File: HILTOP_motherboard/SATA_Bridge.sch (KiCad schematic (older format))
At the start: 36 parts

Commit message: Furthe progress on Schematics, assigned all main footprints using latest libraries, removed unwanted tracking and parts from original PCB layout
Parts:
- C204, C223: renamed from C?; footprint Capacitors_SMD:C_0603 -> Capacitor_SMD:C_0603_1608Metric
- FB10, FB11, FB6, FB7, FB9: renamed from FB?; footprint Resistors_SMD:R_0603 -> Resistor_SMD:R_0603_1608Metric
- R177: renamed from R?; footprint (none) -> Resistor_SMD:R_0603_1608Metric
- U37: renamed from U?; footprint Housings_DFN_QFN:Texas_WQFN-MR-100 -> Devtank_PCB_Lib:PQFP-64_7x7mm_P0.4mm_EP; Devtank (none) -> 118-003
- gave numbers to parts that had none: 27

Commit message: Schematics complete - 1st draft
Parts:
- removed C204, C206, C219: 100nF, Capacitor_SMD:C_0603_1608Metric, symbol C
- removed C208: 1uF, Capacitor_SMD:C_0603_1608Metric, symbol C
- removed C210, C217: 22uF, Capacitor_SMD:C_0805_2012Metric, symbol C
- removed FB10, FB6: 120R_100MHz, Resistor_SMD:R_0603_1608Metric, symbol L
- removed R177: R, Resistor_SMD:R_0603_1608Metric, symbol R
- removed U37: TUSB9260, Devtank_PCB_Lib:PQFP-64_7x7mm_P0.4mm_EP, symbol TUSB9260
- added C204, C206: 9pF, Capacitor_SMD:C_0603_1608Metric, symbol device:C
- added C208, C210: 100nF, Capacitor_SMD:C_0603_1608Metric, symbol device:C
- added D84: STPS1L30, Diode_SMD:D_SMB, symbol device:D
- added D85, D86, D87, D88, D89, D90, D91, D92: GRN, LED_SMD:LED_0603_1608Metric, symbol device:LED
- added J25: DEBUG, Connector_PinHeader_2.54mm:PinHeader_1x03_P2.54mm_Vertical, symbol Connector:Conn_01x03
- added R177, R225, R227, R229: DNF, Resistor_SMD:R_0603_1608Metric, symbol device:R
- added R224, R226, R230, R231: 4K7, Resistor_SMD:R_0603_1608Metric, symbol device:R
- added R228, R233: 10K, Resistor_SMD:R_0603_1608Metric, symbol device:R
- added R232: 0R, Resistor_SMD:R_0603_1608Metric, symbol device:R
- added R234: 90.9K, Resistor_SMD:R_0603_1608Metric, symbol device:R
- added R235, R236, R237, R238, R239, R240, R241, R242: 330R, Resistor_SMD:R_0603_1608Metric, symbol device:R
- added U37: TUSB9261, Devtank_PCB_Lib:PQFP-64_7x7mm_P0.4mm_EP, symbol Devtank:TUSB9261
- added U38: AT25DN512CSSHF-B, Package_SO:SOIC-8_3.9x4.9mm_P1.27mm, symbol memory:AT25_EEPROM
- added Y7: 40MHz Crystal, Crystal:Crystal_SMD_SeikoEpson_FA238V-4Pin_3.2x2.5mm, symbol device:Crystal_GND24
- C195, C196, C197, C198, C199, C200, C201, C202, C203, C205, C207, C209, C211, C212, C213, C214, C215, C216, C218, C220, C221, C222, C223: symbol C -> device:C
- FB11, FB7, FB9: symbol L -> device:L
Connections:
- net labels added: +1V1_SATA, +5V, GPIO_0, GPIO_1, GPIO_2, GPIO_3, GPIO_4, GPIO_5, GPIO_6, GPIO_7
- net labels removed: +1V2_SATA, +1V2_USB2_SATA, +1V8, +1V8_SATA
- wire segments 70 -> 272
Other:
- note added: "Match Tracks to 2.5 Mils\n100Ohms Differential Impedance\n50Ohms Single-ended Impedance"

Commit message: BOM nearly complete!
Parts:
- C195: Devtank (none) -> 105-012
- C196, C221, C222: Devtank (none) -> 105-018
- C197, C198, C199, C200: footprint Resistor_SMD:R_0402_1005Metric -> Capacitor_SMD:C_0402_1005Metric; Devtank (none) -> 105-017
- D85, D86, D87, D88, D89, D90, D91, D92: footprint LED_SMD:LED_0603_1608Metric -> LED_SMD:LED_0402_1005Metric; Devtank (none) -> 110-005
- R235, R236, R237, R238, R239, R240, R241, R242: footprint Resistor_SMD:R_0603_1608Metric -> Resistor_SMD:R_0402_1005Metric
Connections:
- no-connect marks 0 -> 15
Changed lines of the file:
@@
 F 0 "C197" V 2900 1900 50  0000 L CNN
 F 1 "10nF" V 2900 2275 50  0000 L CNN
-F 2 "Resistor_SMD:R_0402_1005Metric" H 2988 2025 50  0001 C CNN
+F 2 "Capacitor_SMD:C_0402_1005Metric" H 2988 2025 50  0001 C CNN
 F 3 "" H 2950 2175 50  0001 C CNN
+F 4 "105-017" V 2950 2175 50  0001 C CNN "Devtank"
 	1    2950 2175
 	0    1    1    0
@@
 F 0 "C198" V 2900 2125 50  0000 L CNN
 F 1 "10nF" V 2900 2500 50  0000 L CNN
-F 2 "Resistor_SMD:R_0402_1005Metric" H 2988 2250 50  0001 C CNN
+F 2 "Capacitor_SMD:C_0402_1005Metric" H 2988 2250 50  0001 C CNN
 F 3 "" H 2950 2400 50  0001 C CNN
+F 4 "105-017" V 2950 2400 50  0001 C CNN "Devtank"
 	1    2950 2400
 	0    1    1    0
@@
 F 0 "C199" V 2900 2350 50  0000 L CNN
 F 1 "10nF" V 2900 2725 50  0000 L CNN
-F 2 "Resistor_SMD:R_0402_1005Metric" H 2988 2475 50  0001 C CNN
+F 2 "Capacitor_SMD:C_0402_1005Metric" H 2988 2475 50  0001 C CNN
 F 3 "" H 2950 2625 50  0001 C CNN
+F 4 "105-017" V 2950 2625 50  0001 C CNN "Devtank"
 	1    2950 2625
 	0    1    1    0
@@
 F 0 "C200" V 2900 2575 50  0000 L CNN
 F 1 "10nF" V 2900 2950 50  0000 L CNN
-F 2 "Resistor_SMD:R_0402_1005Metric" H 2988 2700 50  0001 C CNN
+F 2 "Capacitor_SMD:C_0402_1005Metric" H 2988 2700 50  0001 C CNN
 F 3 "" H 2950 2850 50  0001 C CNN
+F 4 "105-017" V 2950 2850 50  0001 C CNN "Devtank"
 	1    2950 2850
 	0    1    1    0
@@
 F 2 "Capacitor_SMD:C_0805_2012Metric" H 8063 9950 50  0001 C CNN
 F 3 "" H 8025 10100 50  0000 C CNN
+F 4 "105-018" H 8025 10100 50  0001 C CNN "Devtank"
 	1    8025 10100
 	1    0    0    -1
@@
 F 2 "Capacitor_SMD:C_0805_2012Metric" H 8863 9950 50  0001 C CNN
 F 3 "" H 8825 10100 50  0000 C CNN
+F 4 "105-018" H 8825 10100 50  0001 C CNN "Devtank"
 	1    8825 10100
 	1    0    0    -1
@@
 F 2 "Capacitor_SMD:C_0805_2012Metric" H 2688 8100 50  0001 C CNN
 F 3 "" H 2650 8250 50  0000 C CNN
+F 4 "105-018" H 2650 8250 50  0001 C CNN "Devtank"
 	1    2650 8250
 	1    0    0    -1
@@
 F 2 "Capacitor_SMD:C_0603_1608Metric" H 2338 8100 50  0001 C CNN
 F 3 "" H 2300 8250 50  0000 C CNN
+F 4 "105-012" H 2300 8250 50  0001 C CNN "Devtank"
 	1    2300 8250
 	1    0    0    -1
@@
 F 0 "R235" V 11375 6400 50  0000 C CNN
 F 1 "330R" V 11375 6850 50  0000 C CNN
-F 2 "Resistor_SMD:R_0603_1608Metric" V 11355 6625 50  0001 C CNN
+F 2 "Resistor_SMD:R_0402_1005Metric" V 11355 6625 50  0001 C CNN
 F 3 "" H 11425 6625 50  0000 C CNN
 F 4 "101-024" V 11425 6625 60  0001 C CNN "Devtank"
@@
 F 0 "D85" H 10425 6675 50  0000 C CNN
 F 1 "GRN" H 10850 6675 50  0000 C CNN
-F 2 "LED_SMD:LED_0603_1608Metric" H 10625 6625 50  0001 C CNN
+F 2 "LED_SMD:LED_0402_1005Metric" H 10625 6625 50  0001 C CNN
 F 3 "" H 10625 6625 50  0001 C CNN
+F 4 "110-005" H 10625 6625 50  0001 C CNN "Devtank"
 	1    10625 6625
 	1    0    0    -1
@@
 F 0 "R236" V 11375 6600 50  0000 C CNN
 F 1 "330R" V 11375 7050 50  0000 C CNN
-F 2 "Resistor_SMD:R_0603_1608Metric" V 11355 6825 50  0001 C CNN
+F 2 "Resistor_SMD:R_0402_1005Metric" V 11355 6825 50  0001 C CNN
 F 3 "" H 11425 6825 50  0000 C CNN
 F 4 "101-024" V 11425 6825 60  0001 C CNN "Devtank"
@@
 F 0 "D86" H 10425 6875 50  0000 C CNN
 F 1 "GRN" H 10850 6875 50  0000 C CNN
-F 2 "LED_SMD:LED_0603_1608Metric" H 10625 6825 50  0001 C CNN
+F 2 "LED_SMD:LED_0402_1005Metric" H 10625 6825 50  0001 C CNN
 F 3 "" H 10625 6825 50  0001 C CNN
+F 4 "110-005" H 10625 6825 50  0001 C CNN "Devtank"
 	1    10625 6825
 	1    0    0    -1
@@
 F 0 "R237" V 11375 6800 50  0000 C CNN
 F 1 "330R" V 11375 7250 50  0000 C CNN
-F 2 "Resistor_SMD:R_0603_1608Metric" V 11355 7025 50  0001 C CNN
+F 2 "Resistor_SMD:R_0402_1005Metric" V 11355 7025 50  0001 C CNN
 F 3 "" H 11425 7025 50  0000 C CNN
 F 4 "101-024" V 11425 7025 60  0001 C CNN "Devtank"
@@
 F 0 "D87" H 10425 7075 50  0000 C CNN
 F 1 "GRN" H 10850 7075 50  0000 C CNN
-F 2 "LED_SMD:LED_0603_1608Metric" H 10625 7025 50  0001 C CNN
+F 2 "LED_SMD:LED_0402_1005Metric" H 10625 7025 50  0001 C CNN
 F 3 "" H 10625 7025 50  0001 C CNN
+F 4 "110-005" H 10625 7025 50  0001 C CNN "Devtank"
 	1    10625 7025
 	1    0    0    -1
@@
 F 0 "R238" V 11375 7000 50  0000 C CNN
 F 1 "330R" V 11375 7450 50  0000 C CNN
-F 2 "Resistor_SMD:R_0603_1608Metric" V 11355 7225 50  0001 C CNN
+F 2 "Resistor_SMD:R_0402_1005Metric" V 11355 7225 50  0001 C CNN
 F 3 "" H 11425 7225 50  0000 C CNN
 F 4 "101-024" V 11425 7225 60  0001 C CNN "Devtank"
@@
 F 0 "D88" H 10425 7275 50  0000 C CNN
 F 1 "GRN" H 10850 7275 50  0000 C CNN
-F 2 "LED_SMD:LED_0603_1608Metric" H 10625 7225 50  0001 C CNN
+F 2 "LED_SMD:LED_0402_1005Metric" H 10625 7225 50  0001 C CNN
 F 3 "" H 10625 7225 50  0001 C CNN
+F 4 "110-005" H 10625 7225 50  0001 C CNN "Devtank"
 	1    10625 7225
 	1    0    0    -1
@@
 F 0 "R239" V 11375 7200 50  0000 C CNN
 F 1 "330R" V 11375 7650 50  0000 C CNN
-F 2 "Resistor_SMD:R_0603_1608Metric" V 11355 7425 50  0001 C CNN
+F 2 "Resistor_SMD:R_0402_1005Metric" V 11355 7425 50  0001 C CNN
 F 3 "" H 11425 7425 50  0000 C CNN
 F 4 "101-024" V 11425 7425 60  0001 C CNN "Devtank"
@@
 F 0 "D89" H 10425 7475 50  0000 C CNN
 F 1 "GRN" H 10850 7475 50  0000 C CNN
-F 2 "LED_SMD:LED_0603_1608Metric" H 10625 7425 50  0001 C CNN
+F 2 "LED_SMD:LED_0402_1005Metric" H 10625 7425 50  0001 C CNN
 F 3 "" H 10625 7425 50  0001 C CNN
+F 4 "110-005" H 10625 7425 50  0001 C CNN "Devtank"
 	1    10625 7425
 	1    0    0    -1
@@
 F 0 "R240" V 11375 7400 50  0000 C CNN
 F 1 "330R" V 11375 7850 50  0000 C CNN
-F 2 "Resistor_SMD:R_0603_1608Metric" V 11355 7625 50  0001 C CNN
+F 2 "Resistor_SMD:R_0402_1005Metric" V 11355 7625 50  0001 C CNN
 F 3 "" H 11425 7625 50  0000 C CNN
 F 4 "101-024" V 11425 7625 60  0001 C CNN "Devtank"
@@
 F 0 "D90" H 10425 7675 50  0000 C CNN
 F 1 "GRN" H 10850 7675 50  0000 C CNN
-F 2 "LED_SMD:LED_0603_1608Metric" H 10625 7625 50  0001 C CNN
+F 2 "LED_SMD:LED_0402_1005Metric" H 10625 7625 50  0001 C CNN
 F 3 "" H 10625 7625 50  0001 C CNN
+F 4 "110-005" H 10625 7625 50  0001 C CNN "Devtank"
 	1    10625 7625
 	1    0    0    -1
@@
 F 0 "R241" V 11375 7600 50  0000 C CNN
 F 1 "330R" V 11375 8050 50  0000 C CNN
-F 2 "Resistor_SMD:R_0603_1608Metric" V 11355 7825 50  0001 C CNN
+F 2 "Resistor_SMD:R_0402_1005Metric" V 11355 7825 50  0001 C CNN
 F 3 "" H 11425 7825 50  0000 C CNN
 F 4 "101-024" V 11425 7825 60  0001 C CNN "Devtank"
@@
 F 0 "D91" H 10425 7875 50  0000 C CNN
 F 1 "GRN" H 10850 7875 50  0000 C CNN
-F 2 "LED_SMD:LED_0603_1608Metric" H 10625 7825 50  0001 C CNN
+F 2 "LED_SMD:LED_0402_1005Metric" H 10625 7825 50  0001 C CNN
 F 3 "" H 10625 7825 50  0001 C CNN
+F 4 "110-005" H 10625 7825 50  0001 C CNN "Devtank"
 	1    10625 7825
 	1    0    0    -1
@@
 F 0 "R242" V 11375 7800 50  0000 C CNN
 F 1 "330R" V 11375 8250 50  0000 C CNN
-F 2 "Resistor_SMD:R_0603_1608Metric" V 11355 8025 50  0001 C CNN
+F 2 "Resistor_SMD:R_0402_1005Metric" V 11355 8025 50  0001 C CNN
 F 3 "" H 11425 8025 50  0000 C CNN
 F 4 "101-024" V 11425 8025 60  0001 C CNN "Devtank"
@@
 F 0 "D92" H 10425 8075 50  0000 C CNN
 F 1 "GRN" H 10850 8075 50  0000 C CNN
-F 2 "LED_SMD:LED_0603_1608Metric" H 10625 8025 50  0001 C CNN
+F 2 "LED_SMD:LED_0402_1005Metric" H 10625 8025 50  0001 C CNN
 F 3 "" H 10625 8025 50  0001 C CNN
+F 4 "110-005" H 10625 8025 50  0001 C CNN "Devtank"
 	1    10625 8025
 	1    0    0    -1
@@
 Wire Wire Line
 	6875 8425 6875 8700
+NoConn ~ 7975 3250
+NoConn ~ 7975 3350
+NoConn ~ 7975 3450
+NoConn ~ 7975 3550
+NoConn ~ 7975 5250
+NoConn ~ 7975 5350
+NoConn ~ 7975 5550
+NoConn ~ 7975 5650
+NoConn ~ 4100 4050
+NoConn ~ 4100 4150
+NoConn ~ 4100 4400
+NoConn ~ 4100 4500
+NoConn ~ 4100 5575
+NoConn ~ 4900 6250
+NoConn ~ 5200 6250
 $EndSCHEMATC

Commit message: nearly finished placing all parts!
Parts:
- J25: Devtank (none) -> 710-015
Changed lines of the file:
@@
 F 2 "Connector_PinHeader_2.54mm:PinHeader_1x03_P2.54mm_Vertical" H 2675 3950 50  0001 C CNN
 F 3 "" H 2675 3950 50  0001 C CNN
+F 4 "710-015" H 2675 3950 50  0001 C CNN "Devtank"
 	1    2675 3950
 	-1   0    0    -1

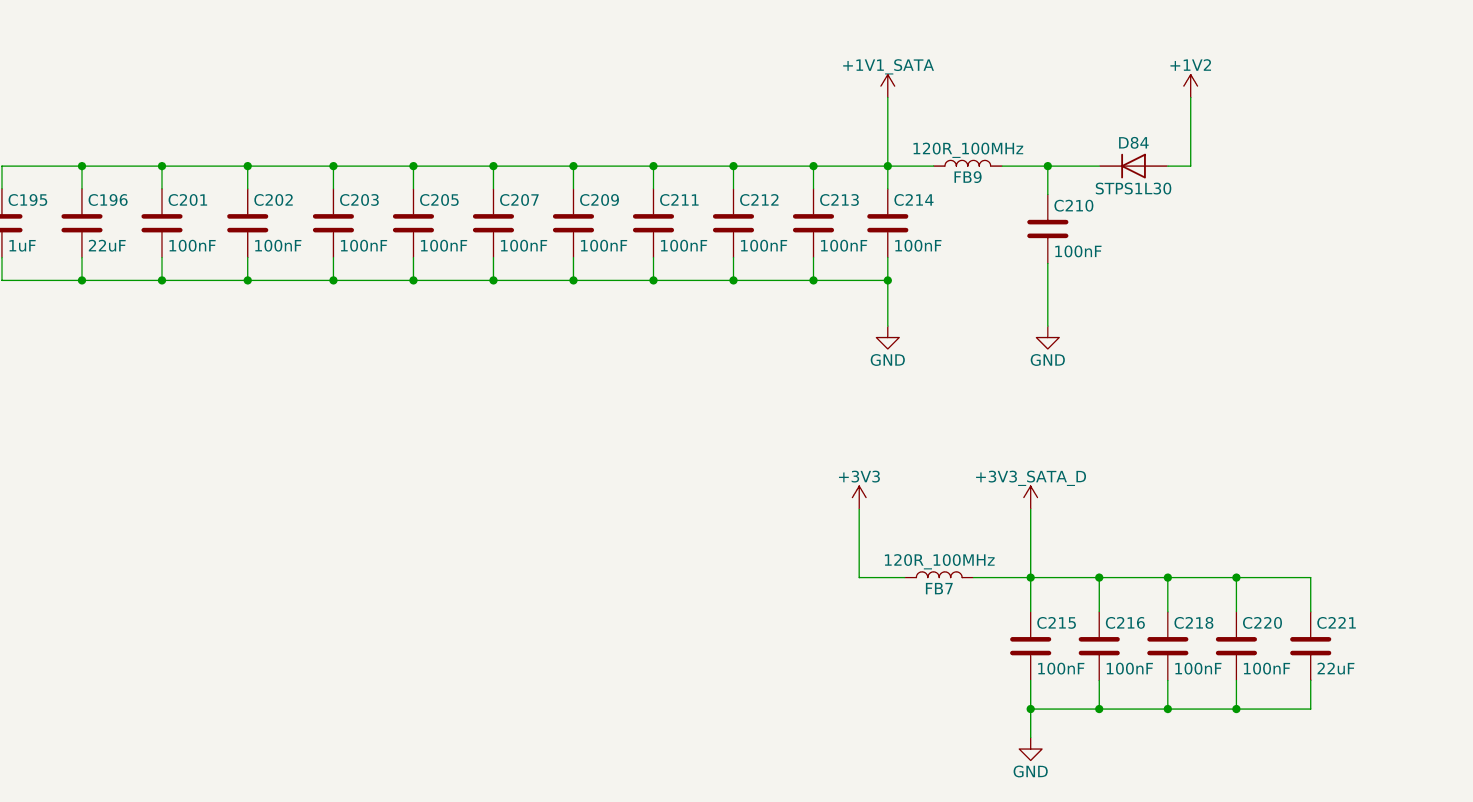
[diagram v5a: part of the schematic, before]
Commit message: All parts placed and backplane connector checked and locked
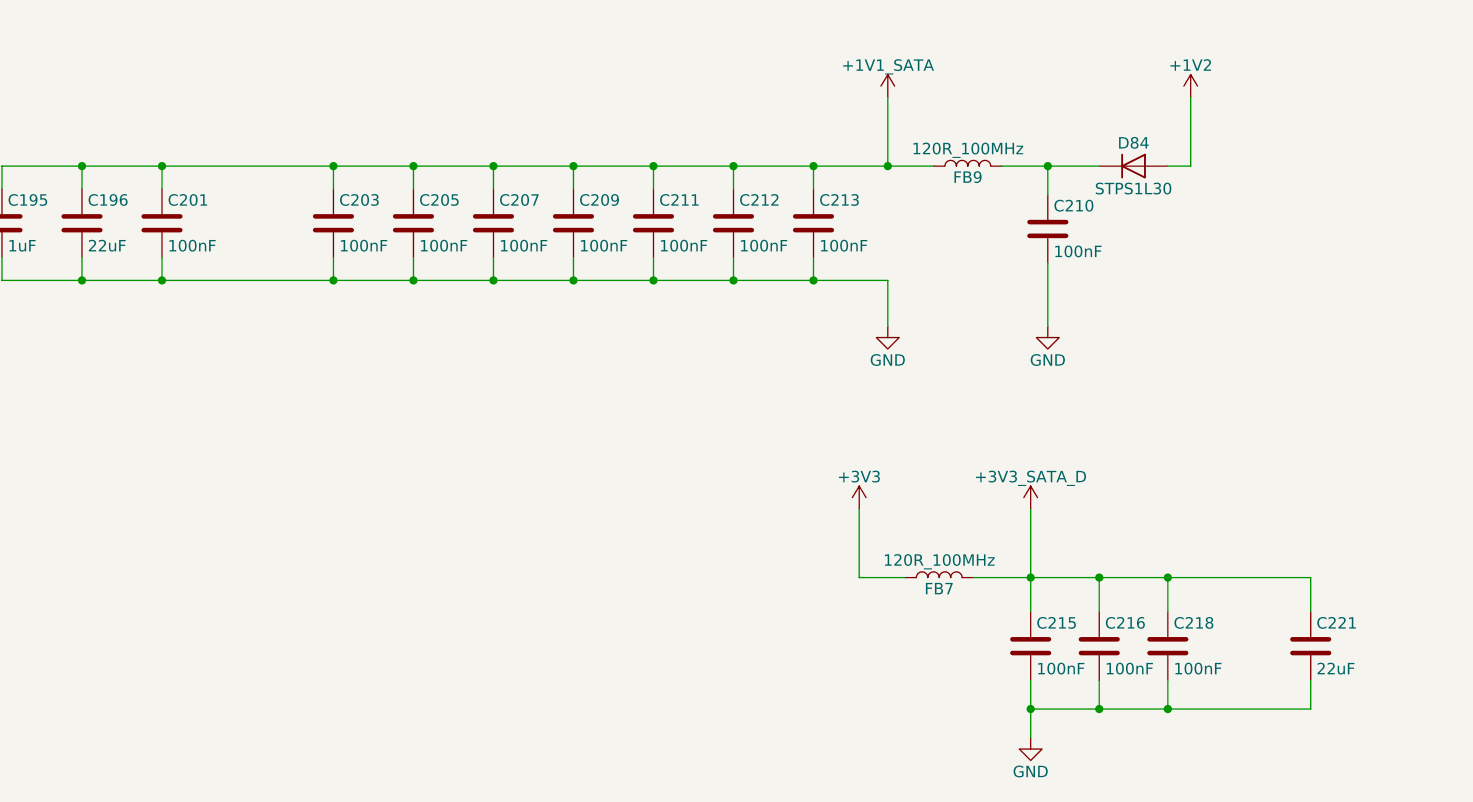
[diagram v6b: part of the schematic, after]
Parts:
- removed C202, C214, C220: 100nF, Capacitor_SMD:C_0603_1608Metric, symbol device:C
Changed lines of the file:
@@
 encoding utf-8
 Sheet 8 12
-Title ""
-Date ""
-Rev ""
-Comp ""
+Title "HILTOP Motherboard"
+Date "2019-01-10"
+Rev "Issue 1"
+Comp "Devtank Ltd"
 Comment1 ""
 Comment2 ""
@@
 $EndComp
 $Comp
-L device:C C214
-U 1 1 5A99EB51
-P 6175 8250
-F 0 "C214" H 6200 8350 50  0000 L CNN
-F 1 "100nF" H 6200 8150 50  0000 L CNN
-F 2 "Capacitor_SMD:C_0603_1608Metric" H 6213 8100 50  0001 C CNN
-F 3 "" H 6175 8250 50  0000 C CNN
-F 4 "105-002" H 6175 8250 60  0001 C CNN "Devtank"
-	1    6175 8250
-	1    0    0    -1
-$EndComp
-$Comp
 L device:C C223
 U 1 1 5A99EB59
@@
 $EndComp
 $Comp
-L device:C C220
-U 1 1 5A9A1EE0
-P 7700 10100
-F 0 "C220" H 7725 10200 50  0000 L CNN
-F 1 "100nF" H 7725 10000 50  0000 L CNN
-F 2 "Capacitor_SMD:C_0603_1608Metric" H 7738 9950 50  0001 C CNN
-F 3 "" H 7700 10100 50  0000 C CNN
-F 4 "105-002" H 7700 10100 60  0001 C CNN "Devtank"
-	1    7700 10100
-	1    0    0    -1
-$EndComp
-$Comp
 L device:C C221
 U 1 1 5A9A1FCA
@@
 $EndComp
 $Comp
-L device:C C202
-U 1 1 5A9A6F30
-P 3375 8250
-F 0 "C202" H 3400 8350 50  0000 L CNN
-F 1 "100nF" H 3400 8150 50  0000 L CNN
-F 2 "Capacitor_SMD:C_0603_1608Metric" H 3413 8100 50  0001 C CNN
-F 3 "" H 3375 8250 50  0000 C CNN
-F 4 "105-002" H 3375 8250 60  0001 C CNN "Devtank"
-	1    3375 8250
-	1    0    0    -1
-$EndComp
-$Comp
 L device:C C201
 U 1 1 5A9A7062
@@
 	9150 9500 9150 9800
 Wire Wire Line
-	6175 8400 6175 8500
-Wire Wire Line
 	2300 8000 2650 8000
 Wire Wire Line
@@
 	7400 9800 7400 9950
 Connection ~ 7100 9800
-Wire Wire Line
-	7700 9800 7700 9950
 Connection ~ 7400 9800
 Wire Wire Line
 	8025 9800 8025 9950
-Connection ~ 7700 9800
 Wire Wire Line
 	7100 10250 7100 10375
@@
 	7400 10375 7400 10250
 Connection ~ 7100 10375
-Wire Wire Line
-	7700 10375 7700 10250
 Connection ~ 7400 10375
 Wire Wire Line
 	8025 10375 8025 10250
-Connection ~ 7700 10375
 Wire Wire Line
 	8825 9950 8825 9800
@@
 Connection ~ 4450 8500
 Connection ~ 4100 8500
-Connection ~ 6175 8500
 Wire Wire Line
 	5850 8400 5850 8500
@@
 	3000 8000 3000 8100
 Wire Wire Line
-	3375 8100 3375 8000
-Connection ~ 3375 8000
-Wire Wire Line
 	3750 8100 3750 8000
 Connection ~ 3750 8000
 Wire Wire Line
 	3750 8400 3750 8500
-Wire Wire Line
-	3375 8500 3375 8400
 Connection ~ 3750 8500
 Wire Wire Line
 	3000 8500 3000 8400
-Connection ~ 3375 8500
 Wire Wire Line
 	2650 8100 2650 8000
@@
 	6175 8000 6375 8000
 Wire Wire Line
-	6175 8000 6175 8100
-Wire Wire Line
 	9150 9800 9350 9800
 Wire Wire Line
@@
 	7100 9800 7400 9800
 Wire Wire Line
-	7400 9800 7700 9800
-Wire Wire Line
-	7700 9800 8025 9800
-Wire Wire Line
 	6800 10375 6800 10500
 Wire Wire Line
 	7100 10375 7400 10375
 Wire Wire Line
-	7400 10375 7700 10375
-Wire Wire Line
-	7700 10375 8025 10375
-Wire Wire Line
 	9150 10375 9150 10500
 Wire Wire Line
@@
 	5850 8000 6175 8000
 Wire Wire Line
-	3375 8000 3750 8000
-Wire Wire Line
 	3750 8000 4100 8000
 Wire Wire Line
 	3750 8500 4100 8500
-Wire Wire Line
-	3375 8500 3750 8500
-Wire Wire Line
-	3000 8000 3375 8000
-Wire Wire Line
-	3000 8500 3375 8500
 Wire Wire Line
 	2650 8500 3000 8500
@@
 NoConn ~ 4900 6250
 NoConn ~ 5200 6250
+Wire Wire Line
+	3000 8500 3750 8500
+Wire Wire Line
+	3000 8000 3750 8000
+Wire Wire Line
+	7400 9800 8025 9800
+Wire Wire Line
+	7400 10375 8025 10375
 $EndSCHEMATC
